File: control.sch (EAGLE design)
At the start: 119 parts, among them IC1 LM358N, IC2 XMEGA16A4A, IC3 LM317MTT3-A, IC5 LM358N, Q1 BSS123, Q10 TIP42C, Q11 BC548, Q12 BC548, Q13 BC557C, Q14 BSS123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

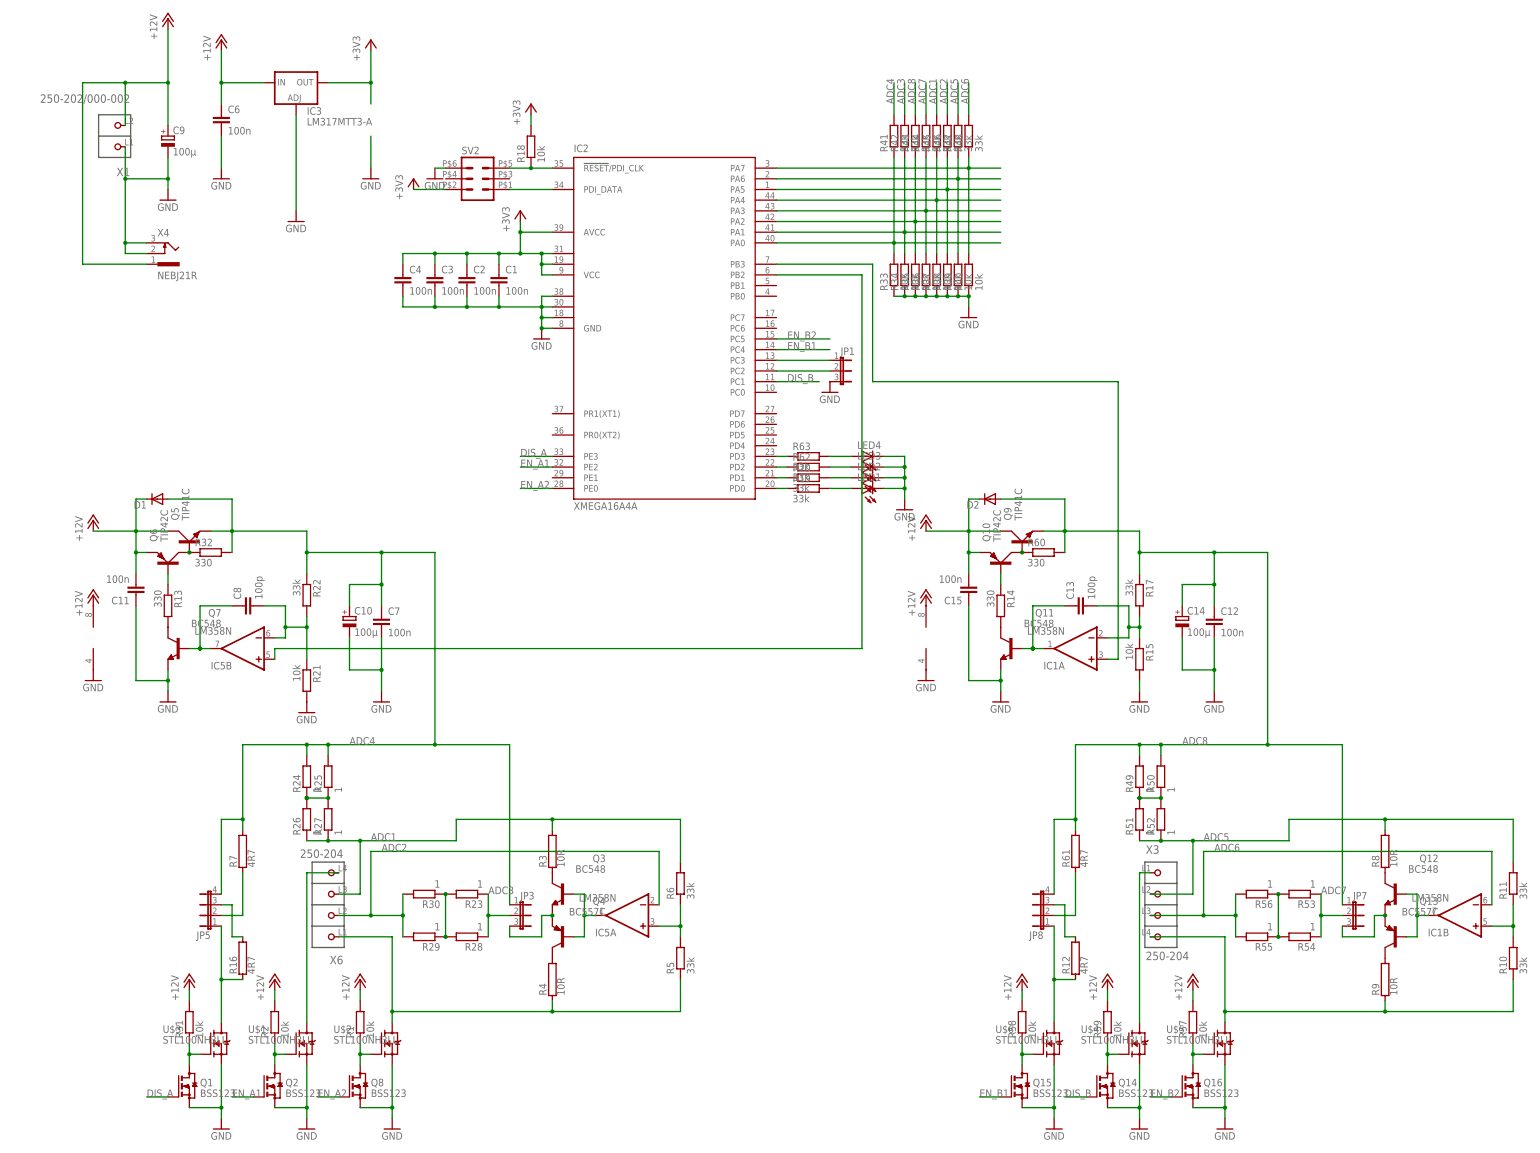
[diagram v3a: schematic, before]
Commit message: author name added
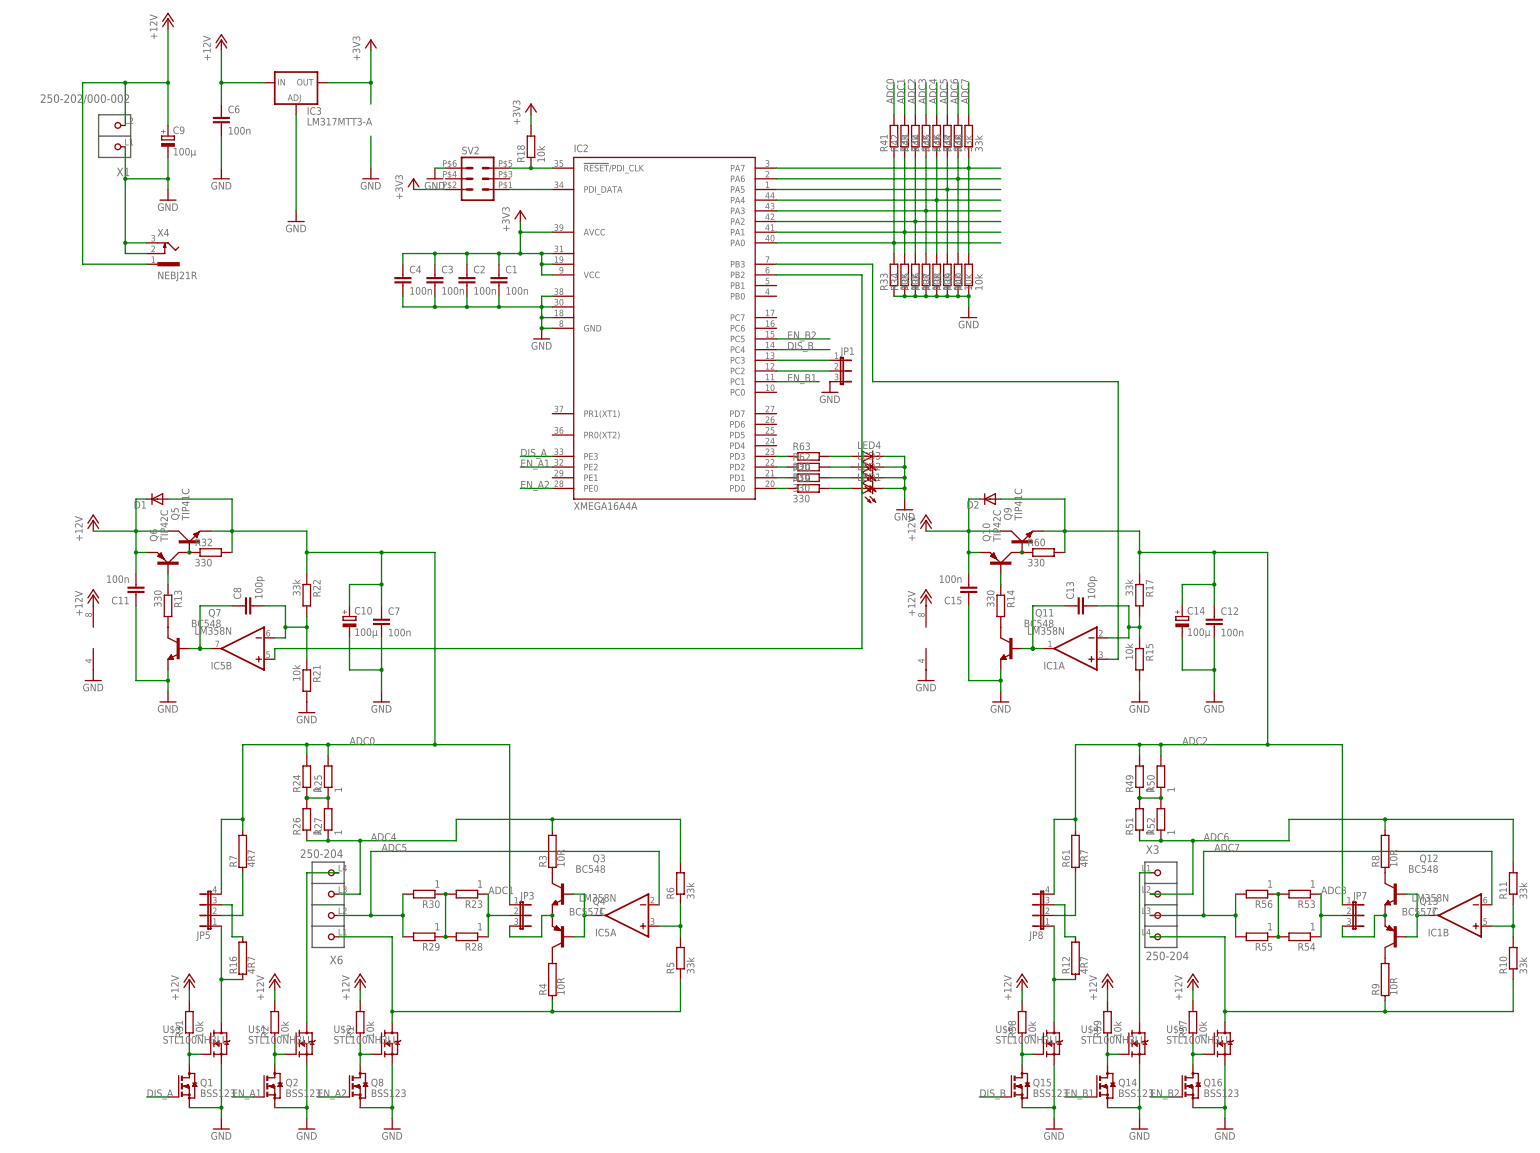
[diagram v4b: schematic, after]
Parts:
- R19, R20, R62, R63: value 33k -> 330
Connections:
- removed net ADC8: C12.1, C14.+, D2.A, JP7.1, JP8.4, Q9.E, R17.1, R43.2, R49.2, R50.2, R60.2, R61.2
- new net ADC0: C10.+, C7.1, D1.A, JP3.1, JP5.4, Q5.E, R22.1, R24.2, R25.2, R32.2, R41.2, R7.2
- net ADC1: now also JP3.2, R23.1, R28.1, R42.2; no longer R26.1, R27.1, R3.2, R45.2, R6.2, X6.P3
- net ADC2: now also C12.1, C14.+, D2.A, JP7.1, JP8.4, Q9.E, R17.1, R43.2, R49.2, R50.2, R60.2, R61.2; no longer IC5A.-IN, R29.2, R30.2, R46.2, X6.P2
- net ADC3: now also JP7.2, R44.2, R53.1, R54.1; no longer JP3.2, R23.1, R28.1, R42.2
- net ADC4: now also R26.1, R27.1, R3.2, R45.2, R6.2, X6.P3; no longer C10.+, C7.1, D1.A, JP3.1, JP5.4, Q5.E, R22.1, R24.2, R25.2, R32.2, R41.2, R7.2
- net ADC5: now also IC5A.-IN, R29.2, R30.2, R46.2, X6.P2; no longer R11.2, R47.2, R51.1, R52.1, R8.2, X3.P2
- net ADC6: now also R11.2, R47.2, R51.1, R52.1, R8.2, X3.P2; no longer IC1B.-IN, R48.2, R55.2, R56.2, X3.P3
- net ADC7: now also IC1B.-IN, R48.2, R55.2, R56.2, X3.P3; no longer JP7.2, R44.2, R53.1, R54.1
- net DIS_B: now also IC2.PC4, Q15.G; no longer IC2.PC1, Q14.G
- net EN_B1: now also IC2.PC1, Q14.G; no longer IC2.PC4, Q15.G
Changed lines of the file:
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@@
 <?xml version="1.0" encoding="utf-8"?>
 <!DOCTYPE eagle SYSTEM "eagle.dtd">
-<eagle version="6.5.0">
+<eagle version="7.6.0">
 <drawing>
 <settings>
@@
 <grid distance="0.1" unitdist="inch" unit="inch" style="lines" multiple="1" display="no" altdistance="0.01" altunitdist="inch" altunit="inch"/>
 <layers>
-<layer number="1" name="Top" color="4" fill="1" visible="yes" active="no"/>
-<layer number="16" name="Bottom" color="1" fill="1" visible="yes" active="no"/>
-<layer number="17" name="Pads" color="2" fill="1" visible="yes" active="no"/>
-<layer number="18" name="Vias" color="2" fill="1" visible="yes" active="no"/>
-<layer number="19" name="Unrouted" color="6" fill="1" visible="yes" active="no"/>
-<layer number="20" name="Dimension" color="15" fill="1" visible="yes" active="no"/>
-<layer number="21" name="tPlace" color="7" fill="1" visible="yes" active="no"/>
-<layer number="22" name="bPlace" color="7" fill="1" visible="yes" active="no"/>
-<layer number="23" name="tOrigins" color="15" fill="1" visible="yes" active="no"/>
-<layer number="24" name="bOrigins" color="15" fill="1" visible="yes" active="no"/>
-<layer number="25" name="tNames" color="7" fill="1" visible="yes" active="no"/>
-<layer number="26" name="bNames" color="7" fill="1" visible="yes" active="no"/>
-<layer number="27" name="tValues" color="7" fill="1" visible="yes" active="no"/>
-<layer number="28" name="bValues" color="7" fill="1" visible="yes" active="no"/>
+<layer number="1" name="Top" color="4" fill="1" visible="no" active="no"/>
+<layer number="16" name="Bottom" color="1" fill="1" visible="no" active="no"/>
+<layer number="17" name="Pads" color="2" fill="1" visible="no" active="no"/>
+<layer number="18" name="Vias" color="2" fill="1" visible="no" active="no"/>
+<layer number="19" name="Unrouted" color="6" fill="1" visible="no" active="no"/>
+<layer number="20" name="Dimension" color="15" fill="1" visible="no" active="no"/>
+<layer number="21" name="tPlace" color="7" fill="1" visible="no" active="no"/>
+<layer number="22" name="bPlace" color="7" fill="1" visible="no" active="no"/>
+<layer number="23" name="tOrigins" color="15" fill="1" visible="no" active="no"/>
+<layer number="24" name="bOrigins" color="15" fill="1" visible="no" active="no"/>
+<layer number="25" name="tNames" color="7" fill="1" visible="no" active="no"/>
+<layer number="26" name="bNames" color="7" fill="1" visible="no" active="no"/>
+<layer number="27" name="tValues" color="7" fill="1" visible="no" active="no"/>
+<layer number="28" name="bValues" color="7" fill="1" visible="no" active="no"/>
 <layer number="29" name="tStop" color="7" fill="3" visible="no" active="no"/>
 <layer number="30" name="bStop" color="7" fill="6" visible="no" active="no"/>
@@
 <layer number="35" name="tGlue" color="7" fill="4" visible="no" active="no"/>
 <layer number="36" name="bGlue" color="7" fill="5" visible="no" active="no"/>
-<layer number="37" name="tTest" color="7" fill="1" visible="yes" active="no"/>
-<layer number="38" name="bTest" color="7" fill="1" visible="yes" active="no"/>
+<layer number="37" name="tTest" color="7" fill="1" visible="no" active="no"/>
+<layer number="38" name="bTest" color="7" fill="1" visible="no" active="no"/>
 <layer number="39" name="tKeepout" color="4" fill="11" visible="no" active="no"/>
 <layer number="40" name="bKeepout" color="1" fill="11" visible="no" active="no"/>
@@
 <layer number="44" name="Drills" color="7" fill="1" visible="no" active="no"/>
 <layer number="45" name="Holes" color="7" fill="1" visible="no" active="no"/>
-<layer number="46" name="Milling" color="3" fill="1" visible="yes" active="no"/>
-<layer number="47" name="Measures" color="7" fill="1" visible="yes" active="no"/>
-<layer number="48" name="Document" color="7" fill="1" visible="yes" active="no"/>
-<layer number="49" name="Reference" color="7" fill="1" visible="yes" active="no"/>
-<layer number="51" name="tDocu" color="7" fill="1" visible="yes" active="no"/>
-<layer number="52" name="bDocu" color="7" fill="1" visible="yes" active="no"/>
+<layer number="46" name="Milling" color="3" fill="1" visible="no" active="no"/>
+<layer number="47" name="Measures" color="7" fill="1" visible="no" active="no"/>
+<layer number="48" name="Document" color="7" fill="1" visible="no" active="no"/>
+<layer number="49" name="Reference" color="7" fill="1" visible="no" active="no"/>
+<layer number="51" name="tDocu" color="7" fill="1" visible="no" active="no"/>
+<layer number="52" name="bDocu" color="7" fill="1" visible="no" active="no"/>
 <layer number="91" name="Nets" color="2" fill="1" visible="yes" active="yes"/>
 <layer number="92" name="Busses" color="1" fill="1" visible="yes" active="yes"/>
@@
 <part name="LED3" library="led" deviceset="LED" device="CHIPLED_0805"/>
 <part name="LED4" library="led" deviceset="LED" device="CHIPLED_0805"/>
-<part name="R19" library="resistor" deviceset="R-EU_" device="M0805" value="33k"/>
-<part name="R20" library="resistor" deviceset="R-EU_" device="M0805" value="33k"/>
-<part name="R62" library="resistor" deviceset="R-EU_" device="M0805" value="33k"/>
-<part name="R63" library="resistor" deviceset="R-EU_" device="M0805" value="33k"/>
+<part name="R19" library="resistor" deviceset="R-EU_" device="M0805" value="330"/>
+<part name="R20" library="resistor" deviceset="R-EU_" device="M0805" value="330"/>
+<part name="R62" library="resistor" deviceset="R-EU_" device="M0805" value="330"/>
+<part name="R63" library="resistor" deviceset="R-EU_" device="M0805" value="330"/>
 <part name="GND9" library="supply1" deviceset="GND" device=""/>
 <part name="X4" library="con-lumberg" deviceset="NEBJ21R" device=""/>
@@
 </segment>
 </net>
-<net name="ADC2" class="0">
+<net name="ADC5" class="0">
 <segment>
 <wire x1="60.96" y1="58.42" x2="68.58" y2="58.42" width="0.1524" layer="91"/>
@@
 </segment>
 </net>
-<net name="ADC1" class="0">
+<net name="ADC4" class="0">
 <segment>
 <wire x1="58.42" y1="63.5" x2="58.42" y2="76.2" width="0.1524" layer="91"/>
@@
 </segment>
 </net>
-<net name="ADC3" class="0">
+<net name="ADC1" class="0">
 <segment>
 <pinref part="JP3" gate="1" pin="2"/>
@@
 </segment>
 </net>
-<net name="ADC4" class="0">
+<net name="ADC0" class="0">
 <segment>
 <pinref part="JP5" gate="G$1" pin="4"/>
@@
 </segment>
 </net>
-<net name="ADC5" class="0">
+<net name="ADC6" class="0">
 <segment>
 <wire x1="256.54" y1="63.5" x2="256.54" y2="76.2" width="0.1524" layer="91"/>
@@
 </segment>
 </net>
-<net name="ADC6" class="0">
+<net name="ADC7" class="0">
 <segment>
 <wire x1="259.08" y1="58.42" x2="266.7" y2="58.42" width="0.1524" layer="91"/>
@@
 </segment>
 </net>
-<net name="ADC7" class="0">
+<net name="ADC3" class="0">
 <segment>
 <pinref part="JP7" gate="1" pin="2"/>
@@
 </segment>
 </net>
-<net name="ADC8" class="0">
+<net name="ADC2" class="0">
 <segment>
 <pinref part="JP8" gate="G$1" pin="4"/>
@@
 </segment>
 </net>
-<net name="DIS_B" class="0">
+<net name="EN_B1" class="0">
 <segment>
 <pinref part="Q14" gate="G$1" pin="G"/>
@@
 </segment>
 </net>
-<net name="EN_B1" class="0">
+<net name="DIS_B" class="0">
 <segment>
 <pinref part="Q15" gate="G$1" pin="G"/>
